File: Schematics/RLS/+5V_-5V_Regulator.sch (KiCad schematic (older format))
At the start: 12 parts, among them U2 LM317T, U3 LM337T

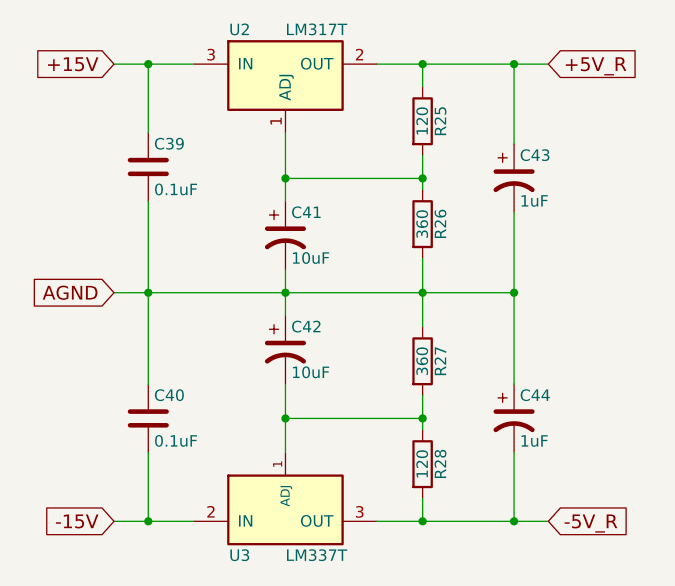
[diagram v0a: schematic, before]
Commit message: Updated schematic (Complete)
Added fan circuit, updated +/- 5V regulated to have 1K pots. Next step is to truly begin the PCB. Will try to have completed by Friday. This will affect our schedule, but we can make up for it in ordering time ¯\_(ツ)_/¯
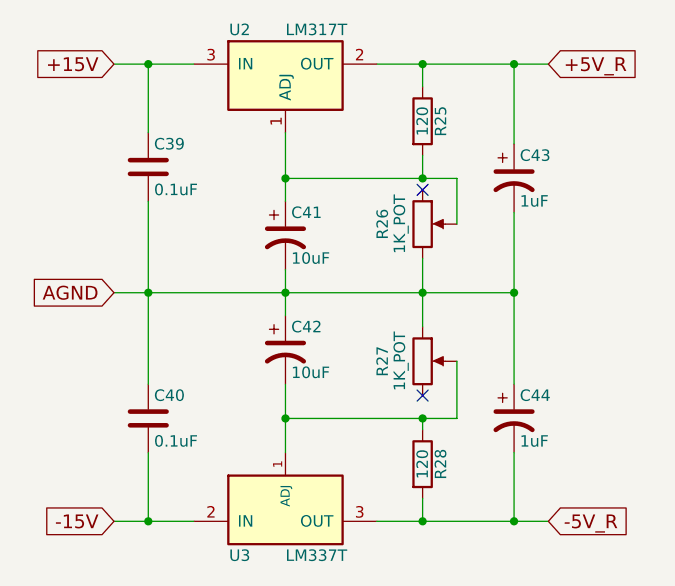
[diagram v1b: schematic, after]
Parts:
- removed R26, R27: 360, symbol R
- added R26, R27: 1K_POT, symbol POT
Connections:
- net AGND: now also R26.3, R27.1
- net at C42.2, R28.1, U3.1 (ADJ): now also R27.2
- net at C41.1, R25.2, U2.1 (ADJ): now also R26.2
- no-connect marks 0 -> 2
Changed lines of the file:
@@
-$EndComp
-$Comp
-L R R26
-U 1 1 595967A8
-P 5500 2400
-AR Path="/5959581C/595967A8" Ref="R26"  Part="1"
-AR Path="/595AEFB9/595967A8" Ref="R26"  Part="1"
-F 0 "R26" V 5580 2400 50  0000 C CNN
-F 1 "360" V 5500 2400 50  0000 C CNN
-F 2 "" V 5430 2400 50  0001 C CNN
-F 3 "" H 5500 2400 50  0001 C CNN
-	1    5500 2400
-	1    0    0    -1
 $EndComp
 $Comp
@@
 	4900 3100 4900 3400
 $Comp
-L R R27
-U 1 1 5959751F
-P 5500 3000
-AR Path="/5959581C/5959751F" Ref="R27"  Part="1"
-AR Path="/595AEFB9/5959751F" Ref="R27"  Part="1"
-F 0 "R27" V 5580 3000 50  0000 C CNN
-F 1 "360" V 5500 3000 50  0000 C CNN
-F 2 "" V 5430 3000 50  0001 C CNN
-F 3 "" H 5500 3000 50  0001 C CNN
-	1    5500 3000
-	1    0    0    -1
-$EndComp
-$Comp
 L R R28
 U 1 1 59597526
@@
 	5300 3700 6050 3700
 Wire Wire Line
-	5500 3300 5500 3150
-Wire Wire Line
 	5500 2550 5500 2850
 Connection ~ 5500 2700
-Wire Wire Line
-	5500 2250 5500 2100
 Wire Wire Line
 	5500 1800 5500 1700
@@
 	5300 1700 6050 1700
 Wire Wire Line
-	5500 2200 4900 2200
+	4900 2200 5650 2200
 Connection ~ 4900 2200
 Connection ~ 5500 2200
 Wire Wire Line
-	5500 3250 4900 3250
+	4900 3250 5650 3250
 Connection ~ 4900 3250
 Connection ~ 5500 3250
@@
 Text GLabel 4150 1700 0    60   Input ~ 0
 +15V
+$Comp
+L POT R26
+U 1 1 595AB1DA
+P 5500 2400
+F 0 "R26" V 5325 2400 50  0000 C CNN
+F 1 "1K_POT" V 5400 2400 50  0000 C CNN
+F 2 "" H 5500 2400 50  0001 C CNN
+F 3 "" H 5500 2400 50  0001 C CNN
+	1    5500 2400
+	1    0    0    -1
+$EndComp
+$Comp
+L POT R27
+U 1 1 595AB23B
+P 5500 3000
+F 0 "R27" V 5325 3000 50  0000 C CNN
+F 1 "1K_POT" V 5400 3000 50  0000 C CNN
+F 2 "" H 5500 3000 50  0001 C CNN
+F 3 "" H 5500 3000 50  0001 C CNN
+	1    5500 3000
+	1    0    0    -1
+$EndComp
+Wire Wire Line
+	5500 2100 5500 2200
+Wire Wire Line
+	5650 2200 5650 2400
+Wire Wire Line
+	5650 3250 5650 3000
+Wire Wire Line
+	5500 3300 5500 3250
+NoConn ~ 5500 3150
+NoConn ~ 5500 2250
 $EndSCHEMATC

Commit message: Most Footprints Added
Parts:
- C39, C40: footprint (none) -> Capacitors_SMD:C_0603_HandSoldering
- C41, C42, C43, C44: footprint (none) -> Capacitors_SMD:CP_Elec_4x5.3
- R25, R28: footprint (none) -> Resistors_SMD:R_1206_HandSoldering
- R26, R27: footprint (none) -> Potentiometers:Potentiometer_Trimmer_Bourns_3296Y
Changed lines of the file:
@@
 F 0 "C41" H 4925 2550 50  0000 L CNN
 F 1 "10uF" H 4925 2350 50  0000 L CNN
-F 2 "" H 4900 2450 50  0001 C CNN
+F 2 "Capacitors_SMD:CP_Elec_4x5.3" H 4900 2450 50  0001 C CNN
 F 3 "" H 4900 2450 50  0001 C CNN
 	1    4900 2450
@@
 F 0 "C39" H 4325 2250 50  0000 L CNN
 F 1 "0.1uF" H 4325 2050 50  0000 L CNN
-F 2 "" H 4338 2000 50  0001 C CNN
+F 2 "Capacitors_SMD:C_0603_HandSoldering" H 4338 2000 50  0001 C CNN
 F 3 "" H 4300 2150 50  0001 C CNN
 	1    4300 2150
@@
 F 0 "R25" V 5580 1950 50  0000 C CNN
 F 1 "120" V 5500 1950 50  0000 C CNN
-F 2 "" V 5430 1950 50  0001 C CNN
+F 2 "Resistors_SMD:R_1206_HandSoldering" V 5430 1950 50  0001 C CNN
 F 3 "" H 5500 1950 50  0001 C CNN
 	1    5500 1950
@@
 F 0 "C40" H 4325 3350 50  0000 L CNN
 F 1 "0.1uF" H 4325 3150 50  0000 L CNN
-F 2 "" H 4338 3100 50  0001 C CNN
+F 2 "Capacitors_SMD:C_0603_HandSoldering" H 4338 3100 50  0001 C CNN
 F 3 "" H 4300 3250 50  0001 C CNN
 	1    4300 3250
@@
 F 0 "C42" H 4925 3050 50  0000 L CNN
 F 1 "10uF" H 4925 2850 50  0000 L CNN
-F 2 "" H 4900 2950 50  0001 C CNN
+F 2 "Capacitors_SMD:CP_Elec_4x5.3" H 4900 2950 50  0001 C CNN
 F 3 "" H 4900 2950 50  0001 C CNN
 	1    4900 2950
@@
 F 0 "R28" V 5580 3450 50  0000 C CNN
 F 1 "120" V 5500 3450 50  0000 C CNN
-F 2 "" V 5430 3450 50  0001 C CNN
+F 2 "Resistors_SMD:R_1206_HandSoldering" V 5430 3450 50  0001 C CNN
 F 3 "" H 5500 3450 50  0001 C CNN
 	1    5500 3450
@@
 F 0 "C43" H 5925 2300 50  0000 L CNN
 F 1 "1uF" H 5925 2100 50  0000 L CNN
-F 2 "" H 5900 2200 50  0001 C CNN
+F 2 "Capacitors_SMD:CP_Elec_4x5.3" H 5900 2200 50  0001 C CNN
 F 3 "" H 5900 2200 50  0001 C CNN
 	1    5900 2200
@@
 F 0 "C44" H 5925 3350 50  0000 L CNN
 F 1 "1uF" H 5925 3150 50  0000 L CNN
-F 2 "" H 5900 3250 50  0001 C CNN
+F 2 "Capacitors_SMD:CP_Elec_4x5.3" H 5900 3250 50  0001 C CNN
 F 3 "" H 5900 3250 50  0001 C CNN
 	1    5900 3250
@@
 F 0 "R26" V 5325 2400 50  0000 C CNN
 F 1 "1K_POT" V 5400 2400 50  0000 C CNN
-F 2 "" H 5500 2400 50  0001 C CNN
+F 2 "Potentiometers:Potentiometer_Trimmer_Bourns_3296Y" H 5500 2400 50  0001 C CNN
 F 3 "" H 5500 2400 50  0001 C CNN
 	1    5500 2400
@@
 F 0 "R27" V 5325 3000 50  0000 C CNN
 F 1 "1K_POT" V 5400 3000 50  0000 C CNN
-F 2 "" H 5500 3000 50  0001 C CNN
+F 2 "Potentiometers:Potentiometer_Trimmer_Bourns_3296Y" H 5500 3000 50  0001 C CNN
 F 3 "" H 5500 3000 50  0001 C CNN
 	1    5500 3000
